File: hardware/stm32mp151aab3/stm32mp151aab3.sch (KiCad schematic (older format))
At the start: 0 parts

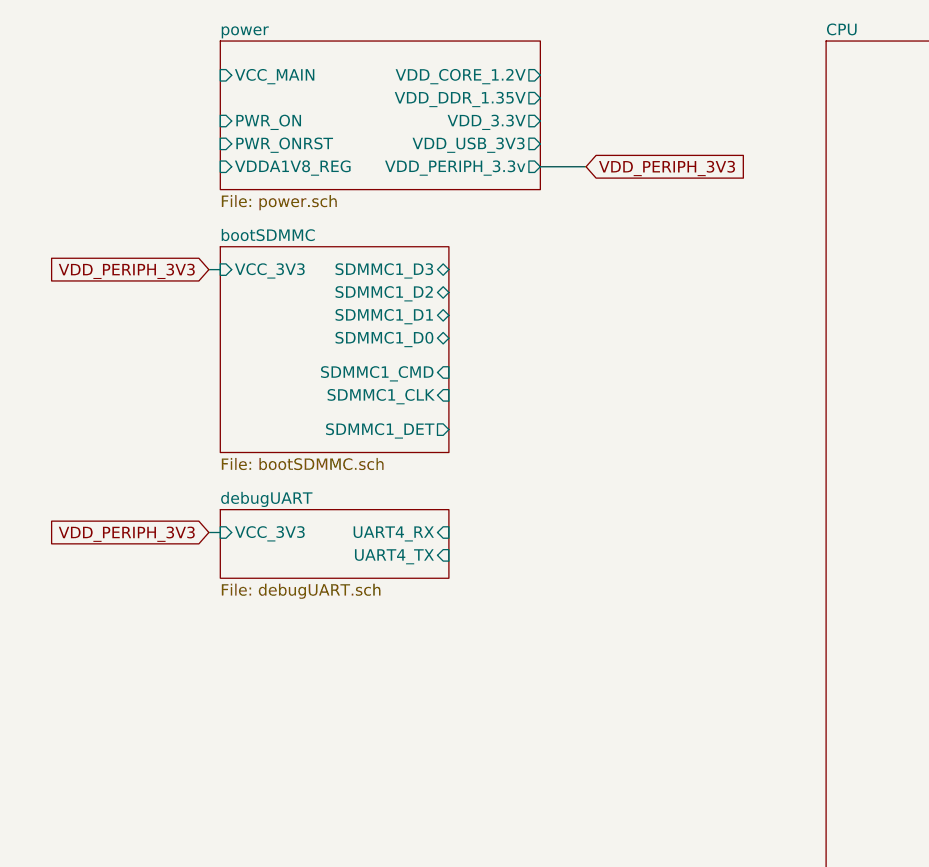
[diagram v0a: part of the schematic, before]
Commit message: add DDR3 page / schematic symbol
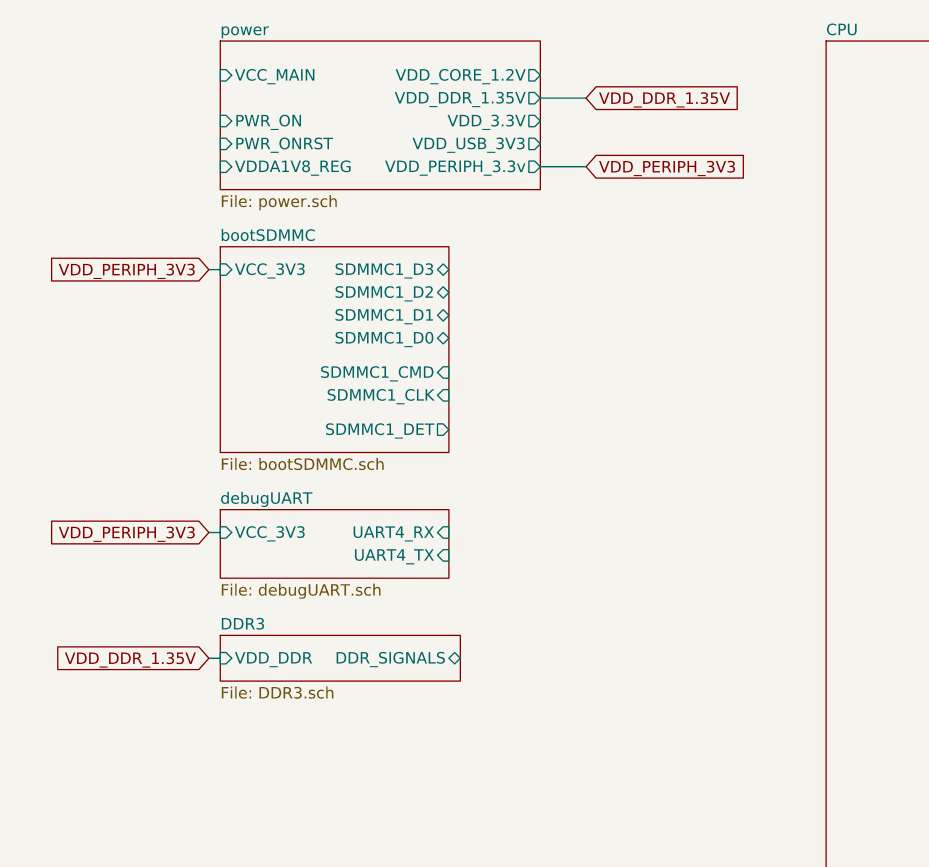
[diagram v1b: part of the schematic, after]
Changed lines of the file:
@@
 $Descr A4 11693 8268
 encoding utf-8
-Sheet 1 5
+Sheet 1 6
 Title ""
 Date ""
@@
 F1 "CPU.sch" 50
 $EndSheet
+$Sheet
+S 1250 3200 1050 200
+U 5FEB1357
+F0 "DDR3" 50
+F1 "DDR3.sch" 50
+F2 "VDD_DDR" I L 1250 3300 50
+F3 "DDR_SIGNALS" B R 2300 3300 50
+$EndSheet
+Text GLabel 2850 850  2    50   Input ~ 0
+VDD_DDR_1.35V
+Wire Wire Line
+	2850 850  2650 850
+Text GLabel 1200 3300 0    50   Input ~ 0
+VDD_DDR_1.35V
+Wire Wire Line
+	1200 3300 1250 3300
 $EndSCHEMATC

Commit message: sch update
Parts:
- added J?: Conn_01x02, symbol Connector_Generic:Conn_01x02
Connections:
- net power/VCC_MAIN: now also J?.1 (Pin_1)
- new net GND: J?.2 (Pin_2)
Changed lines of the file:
@@
 $EndDescr
 $Sheet
-S 1250 600  1400 650
+S 1250 600  1400 1050
 U 5FBDEBA6
 F0 "power" 50
 F1 "power.sch" 50
-F2 "PWR_ON" I L 1250 950 50
-F3 "PWR_ONRST" I L 1250 1050 50
-F4 "VDDA1V8_REG" I L 1250 1150 50
+F2 "PWR_ON" I R 2650 1350 50
+F3 "PWR_ONRST" I R 2650 1450 50
+F4 "VDDA1V8_REG" I R 2650 1550 50
 F5 "VCC_MAIN" I L 1250 750 50
 F6 "VDD_CORE_1.2V" O R 2650 750 50
@@
 $EndSheet
 $Sheet
-S 1250 2650 1000 300
+S 1250 3650 1000 300
 U 5FE704D9
 F0 "debugUART" 50
 F1 "debugUART.sch" 50
-F2 "VCC_3V3" I L 1250 2750 50
-F3 "UART4_RX" I R 2250 2750 50
-F4 "UART4_TX" I R 2250 2850 50
+F2 "VCC_3V3" I L 1250 3750 50
+F3 "UART4_RX" I R 2250 3750 50
+F4 "UART4_TX" I R 2250 3850 50
 $EndSheet
 Text GLabel 2850 1150 2    50   Input ~ 0
@@
 	2850 1150 2650 1150
 Wire Wire Line
-	1200 1600 1250 1600
-Text GLabel 1200 1600 0    50   Input ~ 0
+	1200 2500 1250 2500
+Text GLabel 1200 2500 0    50   Input ~ 0
 VDD_PERIPH_3V3
 $Sheet
-S 1250 1500 1000 900
+S 1250 2400 1000 900
 U 5FE7045F
 F0 "bootSDMMC" 50
 F1 "bootSDMMC.sch" 50
-F2 "VCC_3V3" I L 1250 1600 50
-F3 "SDMMC1_D2" B R 2250 1700 50
-F4 "SDMMC1_D3" B R 2250 1600 50
-F5 "SDMMC1_CMD" I R 2250 2050 50
-F6 "SDMMC1_CLK" I R 2250 2150 50
-F7 "SDMMC1_D0" B R 2250 1900 50
-F8 "SDMMC1_D1" B R 2250 1800 50
-F9 "SDMMC1_DET" O R 2250 2300 50
+F2 "VCC_3V3" I L 1250 2500 50
+F3 "SDMMC1_D2" B R 2250 2600 50
+F4 "SDMMC1_D3" B R 2250 2500 50
+F5 "SDMMC1_CMD" I R 2250 2950 50
+F6 "SDMMC1_CLK" I R 2250 3050 50
+F7 "SDMMC1_D0" B R 2250 2800 50
+F8 "SDMMC1_D1" B R 2250 2700 50
+F9 "SDMMC1_DET" O R 2250 3200 50
 $EndSheet
-Text GLabel 1200 2750 0    50   Input ~ 0
+Text GLabel 1200 3750 0    50   Input ~ 0
 VDD_PERIPH_3V3
 Wire Wire Line
-	1200 2750 1250 2750
+	1200 3750 1250 3750
 $Sheet
-S 3900 600  1750 6800
+S 4000 600  1750 6800
 U 5FE97965
 F0 "CPU" 50
@@
 $EndSheet
 $Sheet
-S 1250 3200 1050 200
+S 1250 4400 1050 200
 U 5FEB1357
 F0 "DDR3" 50
 F1 "DDR3.sch" 50
-F2 "VDD_DDR" I L 1250 3300 50
-F3 "DDR_SIGNALS" B R 2300 3300 50
+F2 "VDD_DDR" I L 1250 4500 50
+F3 "DDR_SIGNALS" B R 2300 4500 50
 $EndSheet
 Text GLabel 2850 850  2    50   Input ~ 0
@@
 Wire Wire Line
 	2850 850  2650 850
-Text GLabel 1200 3300 0    50   Input ~ 0
+Text GLabel 1200 4500 0    50   Input ~ 0
 VDD_DDR_1.35V
 Wire Wire Line
-	1200 3300 1250 3300
+	1200 4500 1250 4500
+$Comp
+L Connector_Generic:Conn_01x02 J?
+U 1 1 6016EFE6
+P 650 750
+F 0 "J?" H 568 967 50  0000 C CNN
+F 1 "Conn_01x02" H 568 876 50  0000 C CNN
+F 2 "" H 650 750 50  0001 C CNN
+F 3 "~" H 650 750 50  0001 C CNN
+	1    650  750
+	-1   0    0    -1
+$EndComp
+$Comp
+L power:GND #PWR?
+U 1 1 6016F7EA
+P 950 950
+F 0 "#PWR?" H 950 700 50  0001 C CNN
+F 1 "GND" H 955 777 50  0000 C CNN
+F 2 "" H 950 950 50  0001 C CNN
+F 3 "" H 950 950 50  0001 C CNN
+	1    950  950
+	1    0    0    -1
+$EndComp
+Wire Wire Line
+	850  850  950  850
+Wire Wire Line
+	950  850  950  950
+Wire Wire Line
+	1250 750  850  750
 $EndSCHEMATC

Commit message: update
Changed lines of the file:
@@
 $Descr A4 11693 8268
 encoding utf-8
-Sheet 1 6
+Sheet 1 7
 Title ""
 Date ""
@@
 $EndDescr
 $Sheet
-S 1250 600  1400 1050
+S 1250 600  1150 1050
 U 5FBDEBA6
 F0 "power" 50
 F1 "power.sch" 50
-F2 "PWR_ON" I R 2650 1350 50
-F3 "PWR_ONRST" I R 2650 1450 50
-F4 "VDDA1V8_REG" I R 2650 1550 50
+F2 "PWR_ON" I R 2400 1350 50
+F3 "PWR_ONRST" I R 2400 1450 50
+F4 "VDDA1V8_REG" I R 2400 1550 50
 F5 "VCC_MAIN" I L 1250 750 50
-F6 "VDD_CORE_1.2V" O R 2650 750 50
-F7 "VDD_DDR_1.35V" O R 2650 850 50
-F8 "VDD_3.3V" O R 2650 950 50
-F9 "VDD_PERIPH_3.3v" O R 2650 1150 50
-F10 "VDD_USB_3V3" O R 2650 1050 50
+F6 "VDD_CORE_1.2V" O R 2400 750 50
+F7 "VDD_DDR_1.35V" O R 2400 850 50
+F8 "VDD_3.3V" O R 2400 950 50
+F9 "VDD_PERIPH_3.3v" O R 2400 1150 50
+F10 "VDD_USB_3V3" O R 2400 1050 50
 $EndSheet
 $Sheet
-S 1250 3650 1000 300
+S 1250 3650 1150 300
 U 5FE704D9
 F0 "debugUART" 50
 F1 "debugUART.sch" 50
 F2 "VCC_3V3" I L 1250 3750 50
-F3 "UART4_RX" I R 2250 3750 50
-F4 "UART4_TX" I R 2250 3850 50
+F3 "UART4_RX" I R 2400 3750 50
+F4 "UART4_TX" I R 2400 3850 50
 $EndSheet
-Text GLabel 2850 1150 2    50   Input ~ 0
+Text GLabel 2600 1150 2    50   Input ~ 0
 VDD_PERIPH_3V3
 Wire Wire Line
-	2850 1150 2650 1150
+	2600 1150 2400 1150
 Wire Wire Line
 	1200 2500 1250 2500
@@
 VDD_PERIPH_3V3
 $Sheet
-S 1250 2400 1000 900
+S 1250 2400 1150 900
 U 5FE7045F
 F0 "bootSDMMC" 50
 F1 "bootSDMMC.sch" 50
 F2 "VCC_3V3" I L 1250 2500 50
-F3 "SDMMC1_D2" B R 2250 2600 50
-F4 "SDMMC1_D3" B R 2250 2500 50
-F5 "SDMMC1_CMD" I R 2250 2950 50
-F6 "SDMMC1_CLK" I R 2250 3050 50
-F7 "SDMMC1_D0" B R 2250 2800 50
-F8 "SDMMC1_D1" B R 2250 2700 50
-F9 "SDMMC1_DET" O R 2250 3200 50
+F3 "SDMMC1_D2" B R 2400 2600 50
+F4 "SDMMC1_D3" B R 2400 2500 50
+F5 "SDMMC1_CMD" I R 2400 2950 50
+F6 "SDMMC1_CLK" I R 2400 3050 50
+F7 "SDMMC1_D0" B R 2400 2800 50
+F8 "SDMMC1_D1" B R 2400 2700 50
+F9 "SDMMC1_DET" O R 2400 3200 50
 $EndSheet
 Text GLabel 1200 3750 0    50   Input ~ 0
@@
 $EndSheet
 $Sheet
-S 1250 4400 1050 200
+S 1250 4400 1150 200
 U 5FEB1357
 F0 "DDR3" 50
 F1 "DDR3.sch" 50
 F2 "VDD_DDR" I L 1250 4500 50
-F3 "DDR_SIGNALS" B R 2300 4500 50
+F3 "DDR_SIGNALS" B R 2400 4500 50
 $EndSheet
-Text GLabel 2850 850  2    50   Input ~ 0
+Text GLabel 2600 850  2    50   Input ~ 0
 VDD_DDR_1.35V
 Wire Wire Line
-	2850 850  2650 850
+	2600 850  2400 850
 Text GLabel 1200 4500 0    50   Input ~ 0
 VDD_DDR_1.35V
@@
 Wire Wire Line
 	1250 750  850  750
+$Sheet
+S 1250 5000 1150 1500
+U 60175391
+F0 "ETHERNET" 50
+F1 "ETHERNET.sch" 50
+F2 "VCC_3V3" I L 1250 5100 50
+F3 "ETH_TXEN" I R 2400 5100 50
+F4 "ETH_TXD0" I R 2400 5200 50
+F5 "ETH_TXD1" I R 2400 5300 50
+F6 "ETH_RXD0" I R 2400 5500 50
+F7 "ETH_RXD1" I R 2400 5600 50
+F8 "ETH_CRS_DV" I R 2400 5700 50
+F9 "ETH_REF_CLK" I R 2400 5800 50
+F10 "ETH_RXER" I R 2400 5900 50
+F11 "ETH_MDIO" I R 2400 6100 50
+F12 "ETH_MDC" I R 2400 6200 50
+F13 "ETH_INTRP" I R 2400 6300 50
+F14 "ETH_~RST" I R 2400 6400 50
+$EndSheet
+Text GLabel 1200 5100 0    50   Input ~ 0
+VDD_PERIPH_3V3
+Wire Wire Line
+	1200 5100 1250 5100
 $EndSCHEMATC
